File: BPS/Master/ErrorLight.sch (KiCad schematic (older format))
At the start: 16 parts, among them J9 ErrorLightConnector, Q3 NTR4003NT1G, Q4 NTR4003NT1G, U14 SI8261ABC-IS

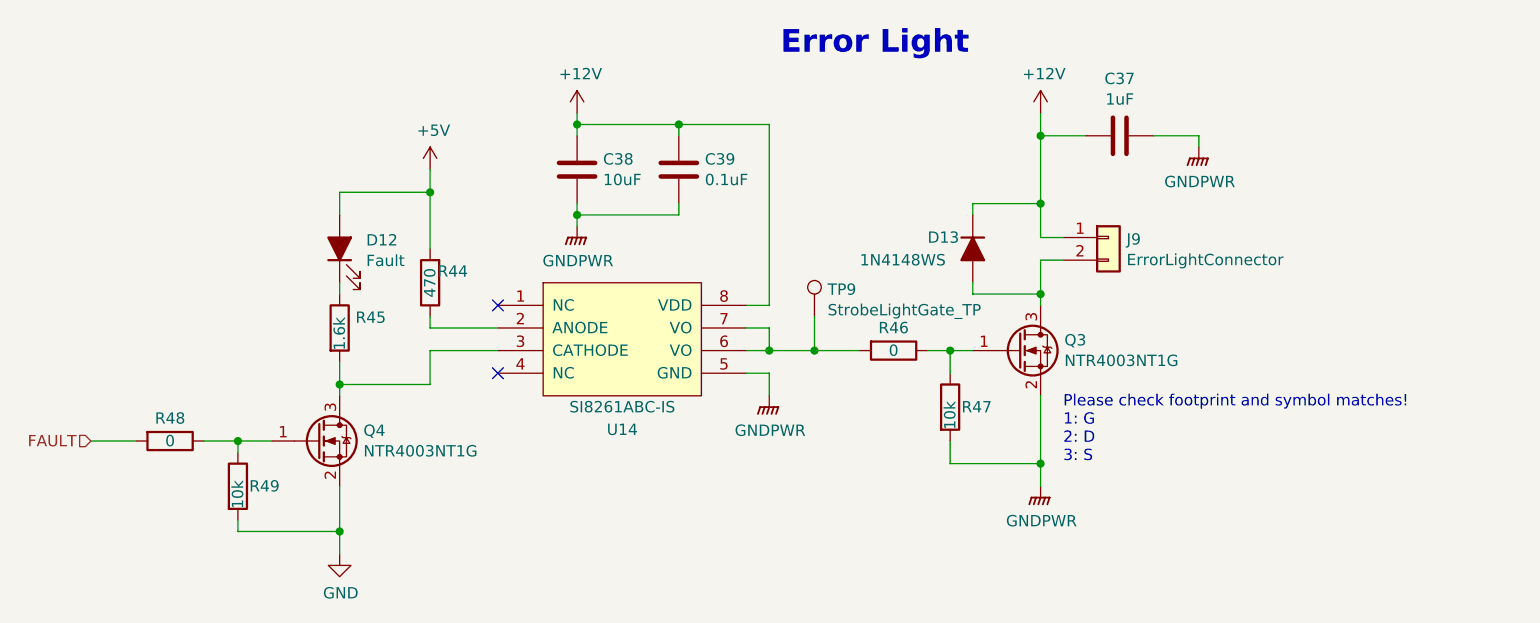
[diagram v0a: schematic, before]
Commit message: Creates fan brd interface schematics and updates symbols/footprints related to the leader board
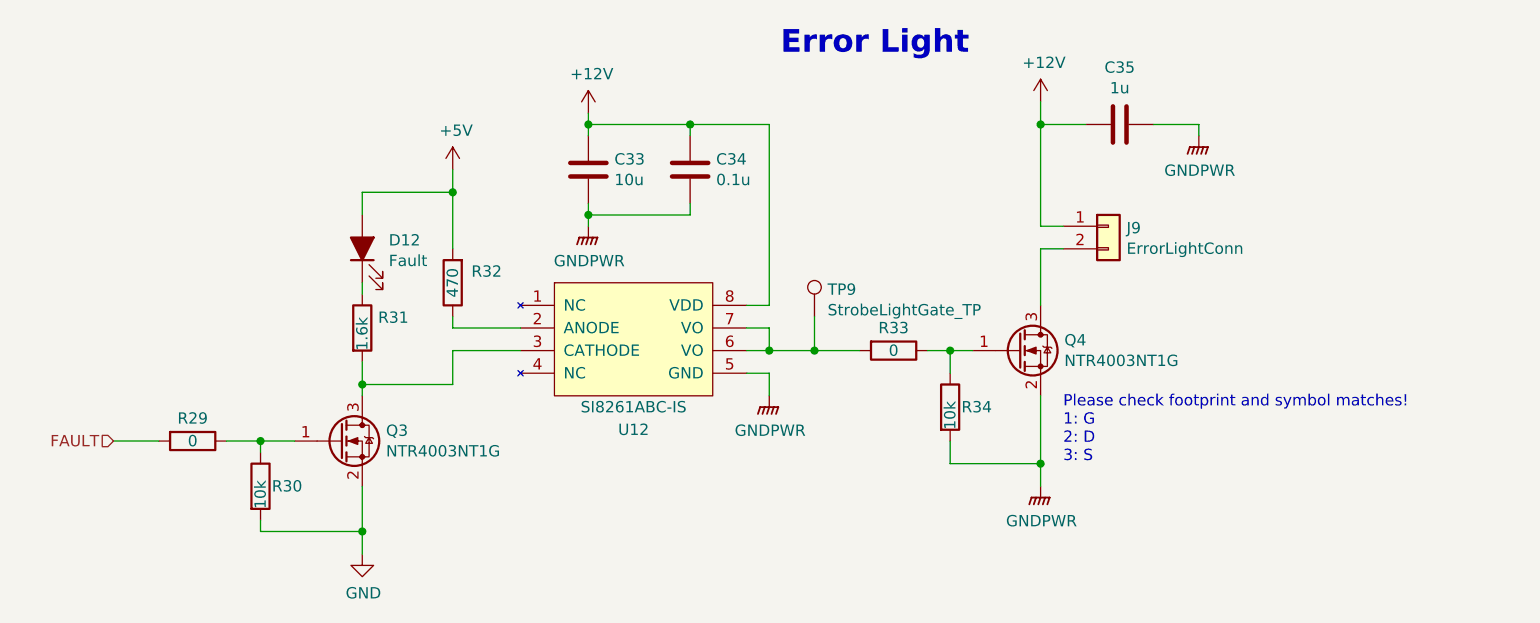
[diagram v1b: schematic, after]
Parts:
- removed D13: 1N4148WS, Diode_SMD:D_SOD-323, symbol Device:D_ALT
- removed U14: SI8261ABC-IS, Package_SO:SOIC-8_3.9x4.9mm_P1.27mm, symbol BPSMaster-rescue:SI8261ABC-IS-utsvt-bps
- added U12: SI8261ABC-IS, Package_SO:SOIC-8_3.9x4.9mm_P1.27mm, symbol utsvt-bps:SI8261ABC-IS
- C33: renamed from C38; value 10uF -> 10u
- C34: renamed from C39; value 0.1uF -> 0.1u
- C35: renamed from C37; value 1uF -> 1u
- J9: value ErrorLightConnector -> ErrorLightConn
- renumbered Q4 to Q3, Q3 to Q4, R48 to R29, R49 to R30, R45 to R31, R44 to R32, R46 to R33, R47 to R34
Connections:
- net +12V: now also U12.8 (VDD)
- net GNDPWR: now also U12.5 (GND)
- net at R32.1: now also U12.2 (ANODE)
- net at Q3.3 (D), R31.2: now also U12.3 (CATHODE)
- net at R33.2, TP9.1: now also U12.6 (VO), U12.7 (VO)
- no-connect marks 2 -> 0
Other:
- moved on the sheet: C33, C34, C35, D12, J9, Q3, R29, R30, R31, R32

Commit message: Finishes schematics for bps leader board
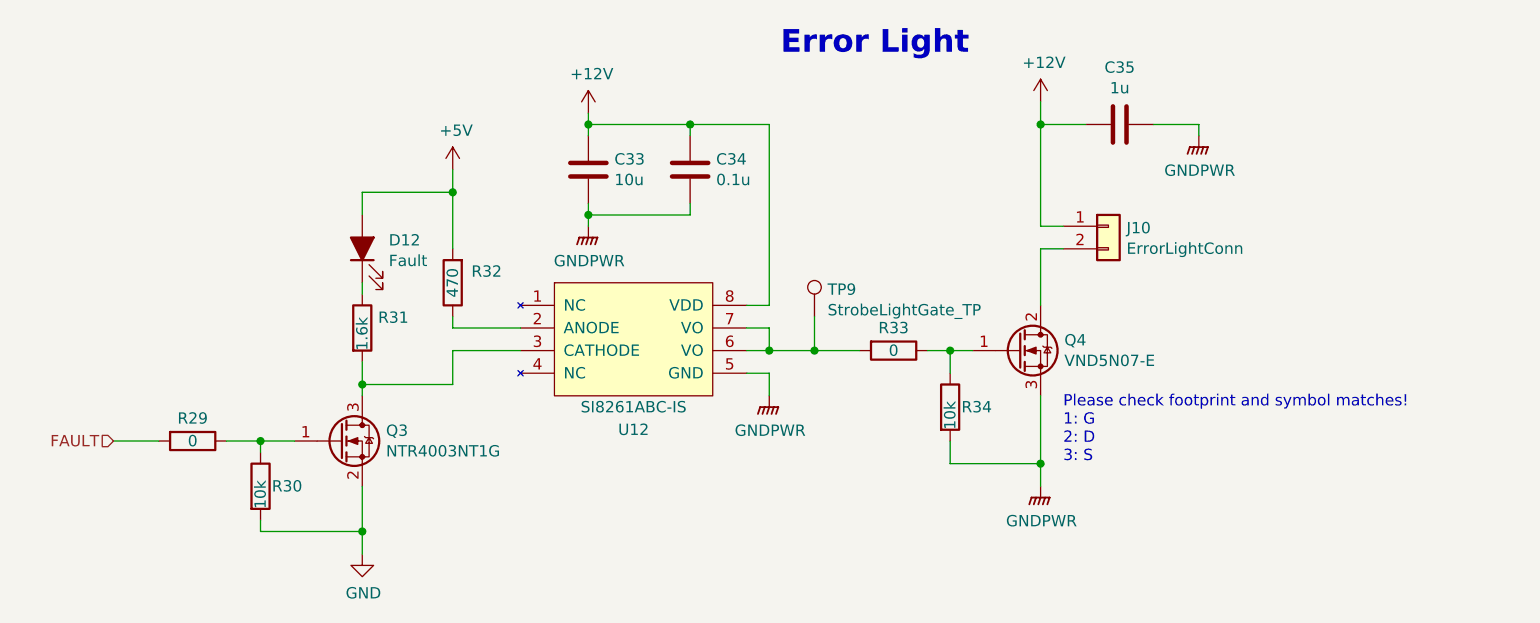
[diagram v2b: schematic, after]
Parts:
- removed Q4: NTR4003NT1G, Package_TO_SOT_SMD:SOT-23, symbol Device:Q_NMOS_GSD
- added Q4: VND5N07-E, Package_TO_SOT_SMD:TO-252-2, symbol Device:Q_NMOS_GDS
- renumbered J9 to J10
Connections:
- net GNDPWR: now also Q4.3 (S)
- net at J10.2 (Pin_2): now also Q4.2 (D)
- net at R33.1, R34.1: now also Q4.1 (G)
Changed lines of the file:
@@
 $Descr A4 11693 8268
 encoding utf-8
-Sheet 8 10
+Sheet 8 11
 Title ""
 Date ""
@@
 P 7350 3400
 AR Path="/5C392C6A/5D93093E" Ref="J?"  Part="1"
-AR Path="/5D923D59/5D93093E" Ref="J9"  Part="1"
-F 0 "J9" H 7430 3392 50  0000 L CNN
+AR Path="/5D923D59/5D93093E" Ref="J10"  Part="1"
+F 0 "J10" H 7430 3392 50  0000 L CNN
 F 1 "ErrorLightConn" H 7430 3301 50  0000 L CNN
 F 2 "UTSVT_Connectors:Molex_MicroFit3.0_1x2xP3.00mm_PolarizingPeg_Vertical" H 7350 3400 50  0001 C CNN
@@
 P 5050 2900
 AR Path="/5C392C6A/5D930954" Ref="#PWR?"  Part="1"
-AR Path="/5D923D59/5D930954" Ref="#PWR065"  Part="1"
-F 0 "#PWR065" H 5050 2750 50  0001 C CNN
+AR Path="/5D923D59/5D930954" Ref="#PWR068"  Part="1"
+F 0 "#PWR068" H 5050 2750 50  0001 C CNN
 F 1 "+12V" H 5065 3073 50  0000 C CNN
 F 2 "" H 5050 2900 50  0001 C CNN
@@
 P 5050 3400
 AR Path="/5C392C6A/5D930960" Ref="#PWR?"  Part="1"
-AR Path="/5D923D59/5D930960" Ref="#PWR066"  Part="1"
-F 0 "#PWR066" H 5050 3200 50  0001 C CNN
+AR Path="/5D923D59/5D930960" Ref="#PWR069"  Part="1"
+F 0 "#PWR069" H 5050 3200 50  0001 C CNN
 F 1 "GNDPWR" H 5054 3246 50  0000 C CNN
 F 2 "" H 5050 3350 50  0001 C CNN
@@
 P 5850 4150
 AR Path="/5C392C6A/5D93097A" Ref="#PWR?"  Part="1"
-AR Path="/5D923D59/5D93097A" Ref="#PWR067"  Part="1"
-F 0 "#PWR067" H 5850 3950 50  0001 C CNN
+AR Path="/5D923D59/5D93097A" Ref="#PWR070"  Part="1"
+F 0 "#PWR070" H 5850 3950 50  0001 C CNN
 F 1 "GNDPWR" H 5854 3996 50  0000 C CNN
 F 2 "" H 5850 4100 50  0001 C CNN
@@
 AR Path="/5C38C674/5D930982" Ref="#PWR?"  Part="1"
 AR Path="/5C392C6A/5D930982" Ref="#PWR?"  Part="1"
-AR Path="/5D923D59/5D930982" Ref="#PWR068"  Part="1"
-F 0 "#PWR068" H 7050 2700 50  0001 C CNN
+AR Path="/5D923D59/5D930982" Ref="#PWR071"  Part="1"
+F 0 "#PWR071" H 7050 2700 50  0001 C CNN
 F 1 "+12V" H 7065 3023 50  0000 C CNN
 F 2 "" H 7050 2850 50  0001 C CNN
@@
 AR Path="/5C38C674/5D9309BC" Ref="#PWR?"  Part="1"
 AR Path="/5C392C6A/5D9309BC" Ref="#PWR?"  Part="1"
-AR Path="/5D923D59/5D9309BC" Ref="#PWR069"  Part="1"
-F 0 "#PWR069" H 7050 4350 50  0001 C CNN
+AR Path="/5D923D59/5D9309BC" Ref="#PWR072"  Part="1"
+F 0 "#PWR072" H 7050 4350 50  0001 C CNN
 F 1 "GNDPWR" H 7054 4396 50  0000 C CNN
 F 2 "" H 7050 4500 50  0001 C CNN
@@
 AR Path="/5C38C674/5D9309C8" Ref="#PWR?"  Part="1"
 AR Path="/5C392C6A/5D9309C8" Ref="#PWR?"  Part="1"
-AR Path="/5D923D59/5D9309C8" Ref="#PWR070"  Part="1"
-F 0 "#PWR070" H 7750 2800 50  0001 C CNN
+AR Path="/5D923D59/5D9309C8" Ref="#PWR073"  Part="1"
+F 0 "#PWR073" H 7750 2800 50  0001 C CNN
 F 1 "GNDPWR" H 7754 2846 50  0000 C CNN
 F 2 "" H 7750 2950 50  0001 C CNN
@@
 	0    -1   -1   0
 $EndComp
-$Comp
-L Device:Q_NMOS_GSD Q?
-U 1 1 5D9309E0
-P 6950 3950
-AR Path="/5C392C6A/5D9309E0" Ref="Q?"  Part="1"
-AR Path="/5D923D59/5D9309E0" Ref="Q4"  Part="1"
-F 0 "Q4" H 7155 3996 50  0000 L CNN
-F 1 "NTR4003NT1G" H 7155 3905 50  0000 L CNN
-F 2 "Package_TO_SOT_SMD:SOT-23" H 7150 4050 50  0001 C CNN
-F 3 "~" H 6950 3950 50  0001 C CNN
-	1    6950 3950
-	1    0    0    -1
-$EndComp
 Wire Wire Line
 	6050 3950 6250 3950
@@
 P 4050 4850
 AR Path="/5C392C6A/5D9309F1" Ref="#PWR?"  Part="1"
-AR Path="/5D923D59/5D9309F1" Ref="#PWR063"  Part="1"
-F 0 "#PWR063" H 4050 4600 50  0001 C CNN
+AR Path="/5D923D59/5D9309F1" Ref="#PWR066"  Part="1"
+F 0 "#PWR066" H 4050 4600 50  0001 C CNN
 F 1 "GND" H 4055 4677 50  0000 C CNN
 F 2 "" H 4050 4850 50  0001 C CNN
@@
 P 4450 3150
 AR Path="/5C392C6A/5D930A01" Ref="#PWR?"  Part="1"
-AR Path="/5D923D59/5D930A01" Ref="#PWR064"  Part="1"
-F 0 "#PWR064" H 4450 3000 50  0001 C CNN
+AR Path="/5D923D59/5D930A01" Ref="#PWR067"  Part="1"
+F 0 "#PWR067" H 4450 3000 50  0001 C CNN
 F 1 "+5V" H 4465 3323 50  0000 C CNN
 F 2 "" H 4450 3150 50  0001 C CNN
@@
 	1    0    0    -1
 $EndComp
+$Comp
+L Device:Q_NMOS_GDS Q?
+U 1 1 5F239C8E
+P 6950 3950
+AR Path="/5C38C674/5F239C8E" Ref="Q?"  Part="1"
+AR Path="/5D923D59/5F239C8E" Ref="Q4"  Part="1"
+F 0 "Q4" H 7155 3996 50  0000 L CNN
+F 1 "VND5N07-E" H 7155 3905 50  0000 L CNN
+F 2 "Package_TO_SOT_SMD:TO-252-2" H 7150 4050 50  0001 C CNN
+F 3 "~" H 6950 3950 50  0001 C CNN
+	1    6950 3950
+	1    0    0    -1
+$EndComp
